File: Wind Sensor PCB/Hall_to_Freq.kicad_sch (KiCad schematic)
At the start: 11 parts, among them U2 TSV911xxLx

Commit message: Large update - firmware and PCB design. V2
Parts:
- C2: LCSC C1804 -> C1729
- D4: LCSC C130247 -> C493206
- R8: LCSC (none) -> C17709
- R9: LCSC C17407 -> C149504; Manufacturer Part MCWR08X1001FTL -> 0805W8F1003T5E

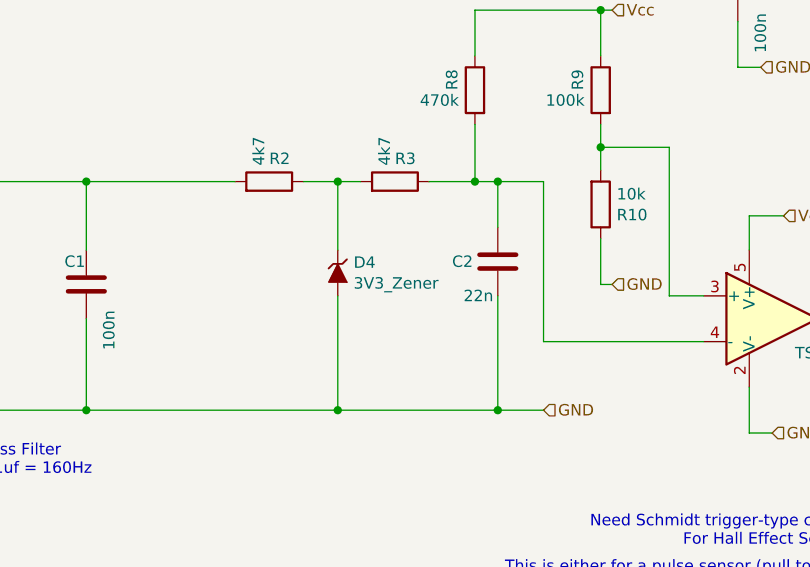
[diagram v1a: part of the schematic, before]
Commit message: Changed to 5V6 zener on all protection
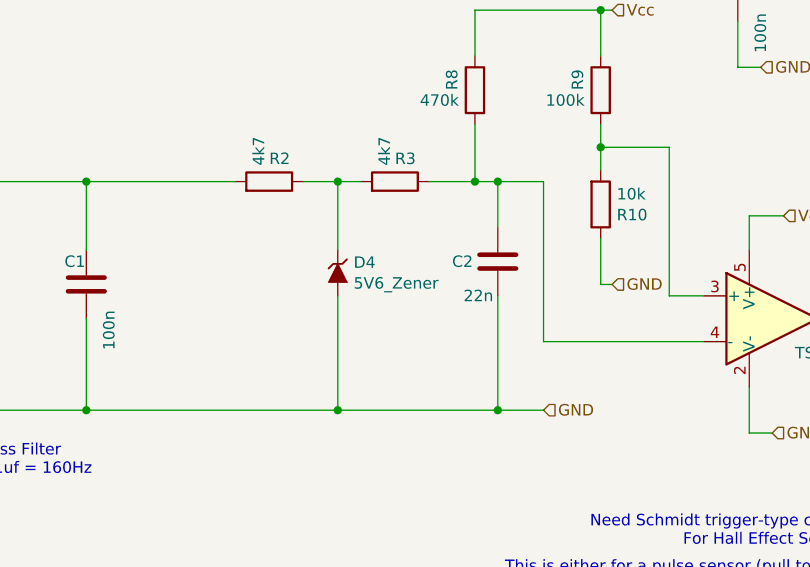
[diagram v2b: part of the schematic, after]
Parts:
- D4: value 3V3_Zener -> 5V6_Zener; LCSC C493206 -> C213355
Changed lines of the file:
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@@
 			)
 		)
-		(property "Value" "3V3_Zener"
+		(property "Value" "5V6_Zener"
 			(at 135.1026 74.803 90)
 			(effects
@@
 			)
 		)
-		(property "LCSC" " C493206"
+		(property "LCSC" " C213355"
 			(at 133.35 73.66 0)
 			(effects

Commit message: updated instructions and schematic files
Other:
- note added: "Hall effect anemometer - between Gnd and SIG Pulse anemometer - between Gnd and SIG NPN output anemometer - between Gnd and SIG This will work for these types"
- note removed: "Hall effect - between Gnd and SIG Pulse between +v and SIG This will work for both"
- note removed: "UPDATED"
- moved on the sheet: C1, C3, R1
